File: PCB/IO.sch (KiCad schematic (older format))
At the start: 56 parts, among them J10 Conn_01x10, J11 10103594-0001LF, J3 105133-0011, J4 10103594-0001LF, J5 NPPN101BFCN-RC, J6 NPPN101BFCN-RC, J7 Conn_01x03, J8 PPTC081LFBN-RC, J9 PPTC081LFBN-RC, Q12 DMG1026UV-7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

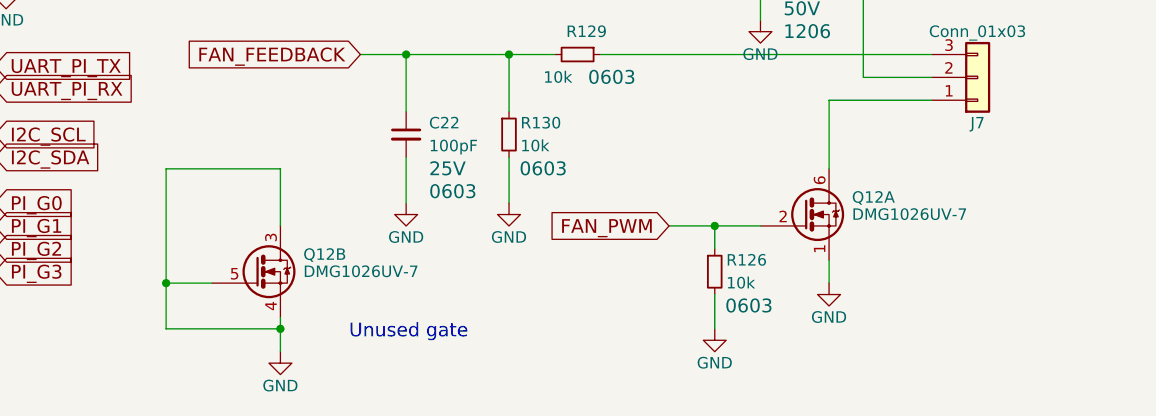
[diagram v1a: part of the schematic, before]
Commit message: Added ELOAD to sch and imported to layout
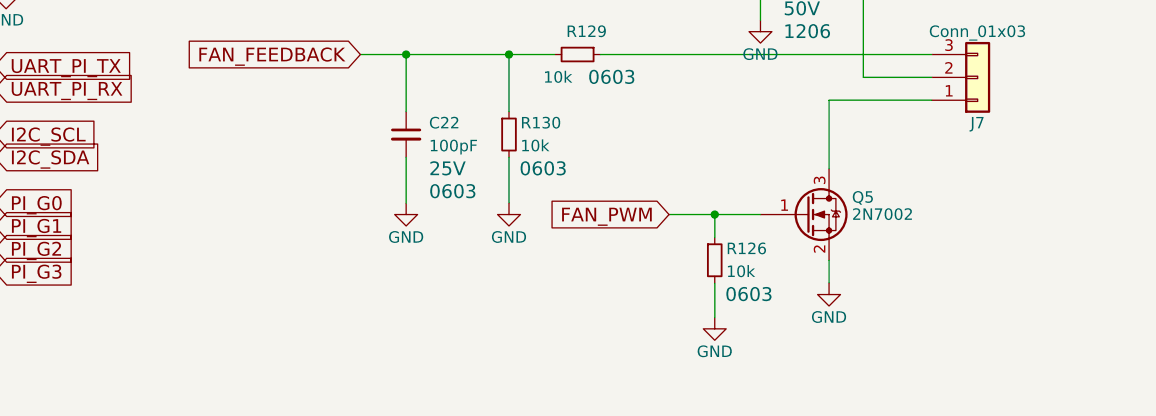
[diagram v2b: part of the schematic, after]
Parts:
- removed Q12: DMG1026UV-7, digikey-footprints:SOT-563, symbol DMG1026UV-7
- added Q5: 2N7002, TO_SOT_Packages_SMD:SOT-23, symbol 2N7002
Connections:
- net FAN_PWM: now also Q5.1 (G)
- net GND: now also Q5.2 (S)
- net at J7.1 (Pin_1): now also Q5.3 (D)
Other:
- note removed: "Unused gate"
- moved on the sheet: R126

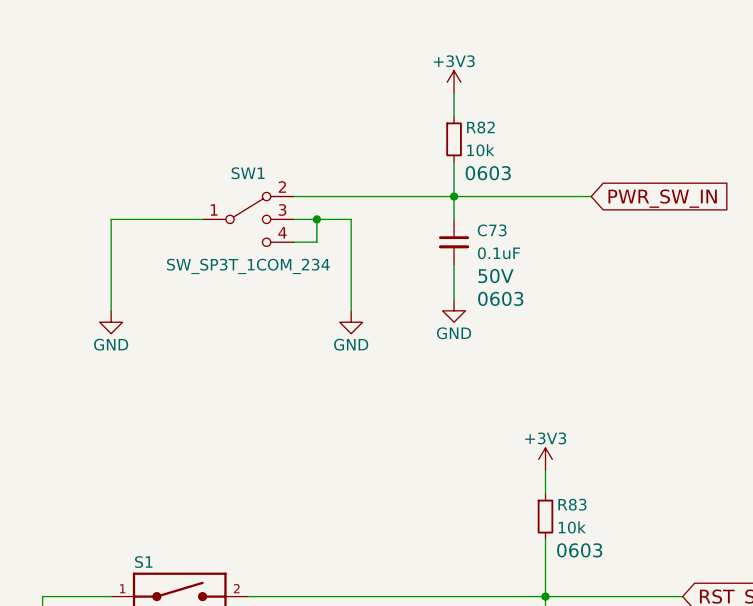
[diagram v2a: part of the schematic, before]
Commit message: Updated switch, need to re-position for alignment...
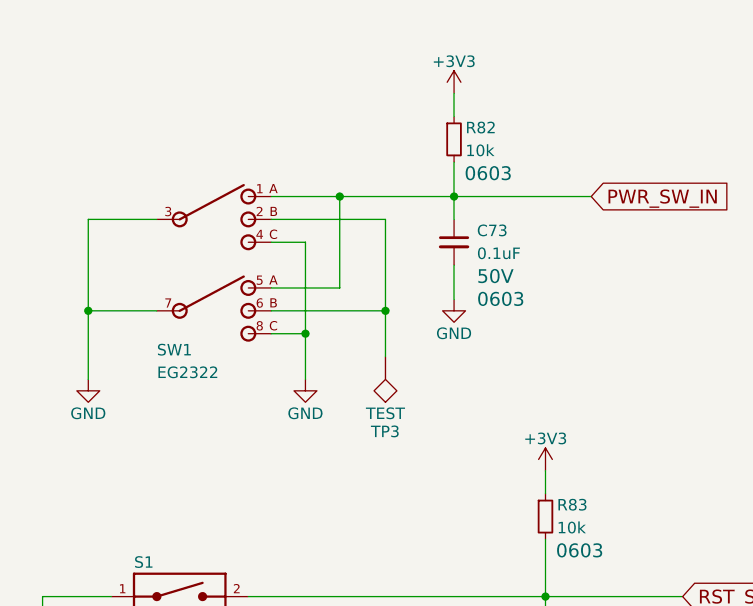
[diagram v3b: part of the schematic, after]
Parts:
- removed SW1: SW_SP3T_1COM_234, CustomFootprints:OS103011MA7QP1, symbol SW_SP3T_1COM_234
- added SW1: EG2322, CustomFootprints:EG2322, symbol CL-SB-23A-01
- added TP3: TEST, Measurement_Points:Measurement_Point_Round-SMD-Pad_Small, symbol TEST
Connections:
- net GND: now also SW1.3, SW1.4, SW1.7, SW1.8
- net PWR_SW_IN: now also SW1.1, SW1.5
- new net: SW1.2, SW1.6, TP3.1
